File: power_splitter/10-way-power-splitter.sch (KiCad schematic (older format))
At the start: 33 parts, among them J1 Conn_01x02, J10 Conn_01x02, J11 Conn_01x02, J2 Conn_01x02, J3 Conn_01x02, J4 Conn_01x02, J5 Conn_01x02, J6 Conn_01x02, J7 Conn_01x02, J8 Conn_01x02, J9 Conn_01x02

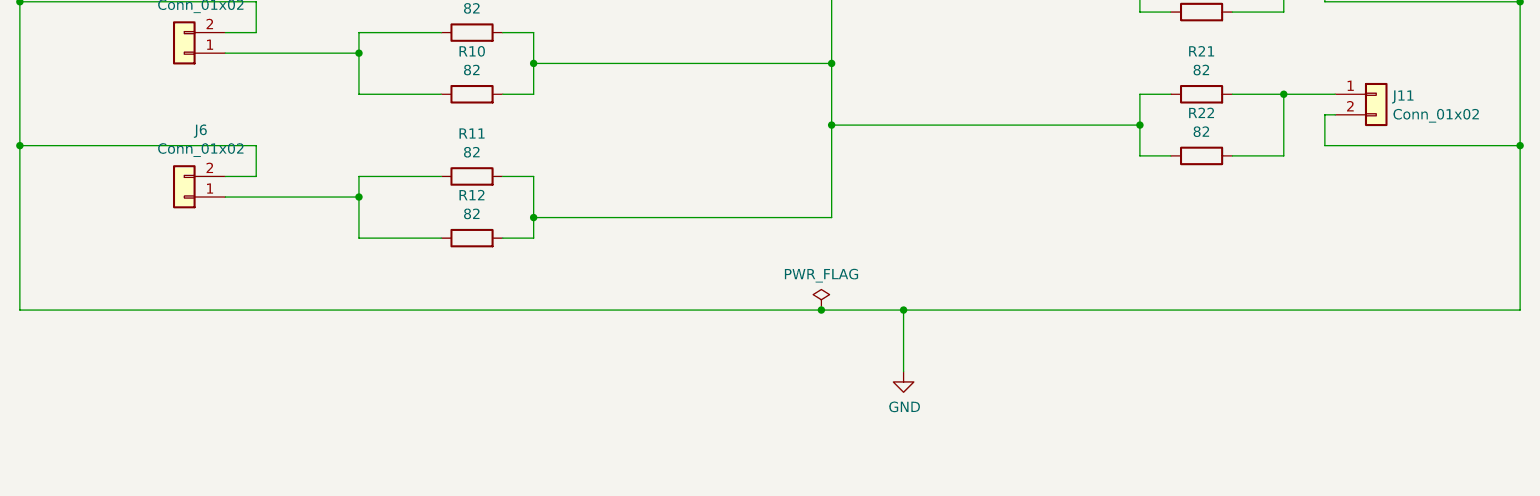
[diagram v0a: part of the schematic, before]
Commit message: power splitter: add a 12th output
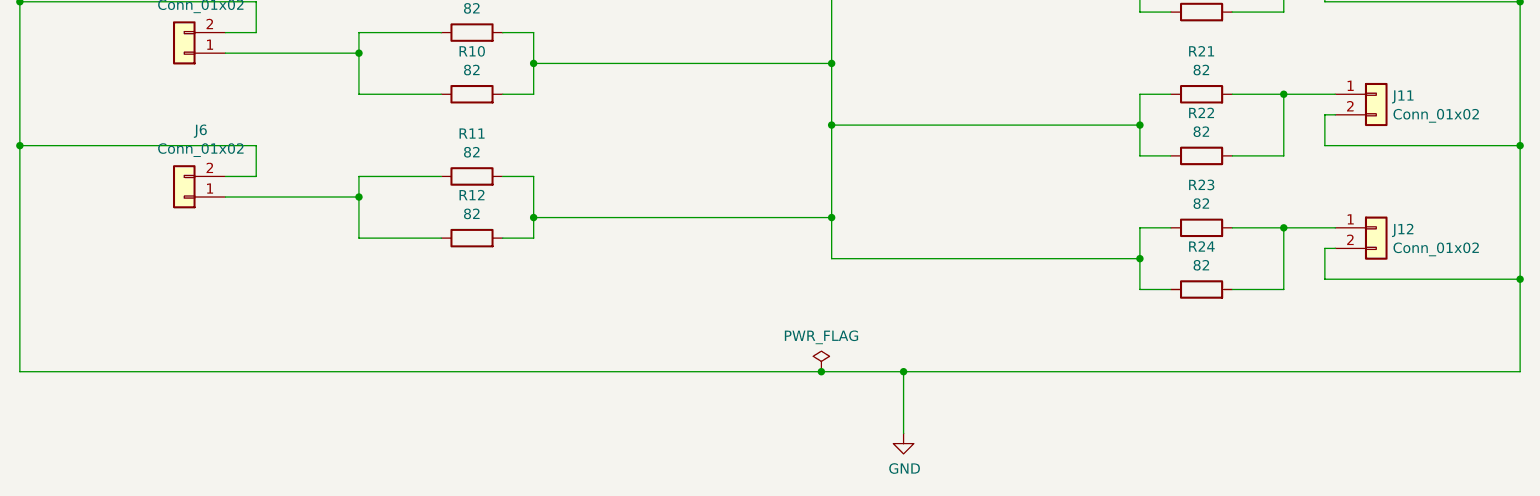
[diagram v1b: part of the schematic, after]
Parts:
- added J12: Conn_01x02, symbol Connector_Generic:Conn_01x02
- added R23, R24: 82, Resistor_SMD:R_0402_1005Metric, symbol Device:R
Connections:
- net GND: now also J12.2 (Pin_2)
- net at R1.2, R10.2, R11.2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: now also R23.1, R24.1
- new net: J12.1 (Pin_1), R23.2, R24.2
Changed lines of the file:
@@
 encoding utf-8
 Sheet 1 1
-Title "10-Way Symmetrical Resisitive Wye Power Splitter"
+Title "11-Way Symmetrical Resisitive Wye Power Splitter"
 Date "20210806"
 Rev "0.1"
@@
 L power:GND #PWR0101
 U 1 1 610F3E57
-P 5150 5800
-F 0 "#PWR0101" H 5150 5550 50  0001 C CNN
-F 1 "GND" H 5155 5627 50  0000 C CNN
-F 2 "" H 5150 5800 50  0001 C CNN
-F 3 "" H 5150 5800 50  0001 C CNN
-	1    5150 5800
+P 5150 6100
+F 0 "#PWR0101" H 5150 5850 50  0001 C CNN
+F 1 "GND" H 5155 5927 50  0000 C CNN
+F 2 "" H 5150 6100 50  0001 C CNN
+F 3 "" H 5150 6100 50  0001 C CNN
+	1    5150 6100
 	1    0    0    -1
 $EndComp
@@
 	2050 1200 850  1200
 Wire Wire Line
-	850  5500 4750 5500
-Wire Wire Line
-	5150 5500 5150 5800
+	850  5800 4750 5800
+Wire Wire Line
+	5150 5800 5150 6100
 Wire Wire Line
 	1850 4850 2000 4850
@@
 Wire Wire Line
 	2000 4700 850  4700
-Connection ~ 850  4700
-Wire Wire Line
-	850  4700 850  5500
 Wire Wire Line
 	1850 4150 2000 4150
@@
 	7200 1950 8150 1950
 Wire Wire Line
-	8150 5500 5150 5500
-Connection ~ 5150 5500
+	8150 5800 5150 5800
+Connection ~ 5150 5800
 Wire Wire Line
 	7250 2450 7200 2450
@@
 Connection ~ 8150 4700
 Wire Wire Line
-	8150 4700 8150 5500
+	8150 4700 8150 5350
 Wire Wire Line
 	8150 4000 8150 4700
@@
 L power:PWR_FLAG #FLG0101
 U 1 1 6125996F
-P 4750 5500
-F 0 "#FLG0101" H 4750 5575 50  0001 C CNN
-F 1 "PWR_FLAG" H 4750 5673 50  0000 C CNN
-F 2 "" H 4750 5500 50  0001 C CNN
-F 3 "~" H 4750 5500 50  0001 C CNN
-	1    4750 5500
+P 4750 5800
+F 0 "#FLG0101" H 4750 5875 50  0001 C CNN
+F 1 "PWR_FLAG" H 4750 5973 50  0000 C CNN
+F 2 "" H 4750 5800 50  0001 C CNN
+F 3 "~" H 4750 5800 50  0001 C CNN
+	1    4750 5800
 	1    0    0    -1
 $EndComp
-Connection ~ 4750 5500
-Wire Wire Line
-	4750 5500 5150 5500
+Connection ~ 4750 5800
+Wire Wire Line
+	4750 5800 5150 5800
+$Comp
+L Device:R R23
+U 1 1 613C2E94
+P 6600 5100
+F 0 "R23" V 6807 5100 50  0000 C CNN
+F 1 "82" V 6716 5100 50  0000 C CNN
+F 2 "Resistor_SMD:R_0402_1005Metric" V 6530 5100 50  0001 C CNN
+F 3 "~" H 6600 5100 50  0001 C CNN
+	1    6600 5100
+	0    -1   -1   0
+$EndComp
+$Comp
+L Device:R R24
+U 1 1 613C2E9A
+P 6600 5400
+F 0 "R24" V 6807 5400 50  0000 C CNN
+F 1 "82" V 6716 5400 50  0000 C CNN
+F 2 "Resistor_SMD:R_0402_1005Metric" V 6530 5400 50  0001 C CNN
+F 3 "~" H 6600 5400 50  0001 C CNN
+	1    6600 5400
+	0    -1   -1   0
+$EndComp
+$Comp
+L Connector_Generic:Conn_01x02 J12
+U 1 1 613C2EA0
+P 7450 5100
+F 0 "J12" H 7530 5092 50  0000 L CNN
+F 1 "Conn_01x02" H 7530 5001 50  0000 L CNN
+F 2 "" H 7450 5100 50  0001 C CNN
+F 3 "~" H 7450 5100 50  0001 C CNN
+	1    7450 5100
+	1    0    0    -1
+$EndComp
+Wire Wire Line
+	7250 5100 7000 5100
+Wire Wire Line
+	7000 5100 7000 5400
+Wire Wire Line
+	7000 5400 6750 5400
+Connection ~ 7000 5100
+Wire Wire Line
+	7000 5100 6750 5100
+Wire Wire Line
+	7250 5200 7200 5200
+Wire Wire Line
+	7200 5350 8150 5350
+Wire Wire Line
+	6450 5400 6300 5400
+Wire Wire Line
+	7200 5200 7200 5350
+Wire Wire Line
+	6300 5100 6450 5100
+Wire Wire Line
+	6300 5400 6300 5250
+Wire Wire Line
+	6300 5250 4800 5250
+Connection ~ 6300 5250
+Wire Wire Line
+	6300 5250 6300 5100
+Wire Wire Line
+	8150 5350 8150 5800
+Connection ~ 8150 5350
+Wire Wire Line
+	850  4700 850  5800
+Connection ~ 850  4700
+Wire Wire Line
+	4800 5250 4800 5050
+Connection ~ 4800 5050
 $EndSCHEMATC
